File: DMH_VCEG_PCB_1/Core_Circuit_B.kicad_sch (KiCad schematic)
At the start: 83 parts, among them Q5 BC548, Q6 BC558, Q7 BC548, SW2 SW_DPDT_x2, U10 TL074, U11 4001, U12 40106, U13 CD4066BE, U14 TL074, U15 TL074, U16 TL074

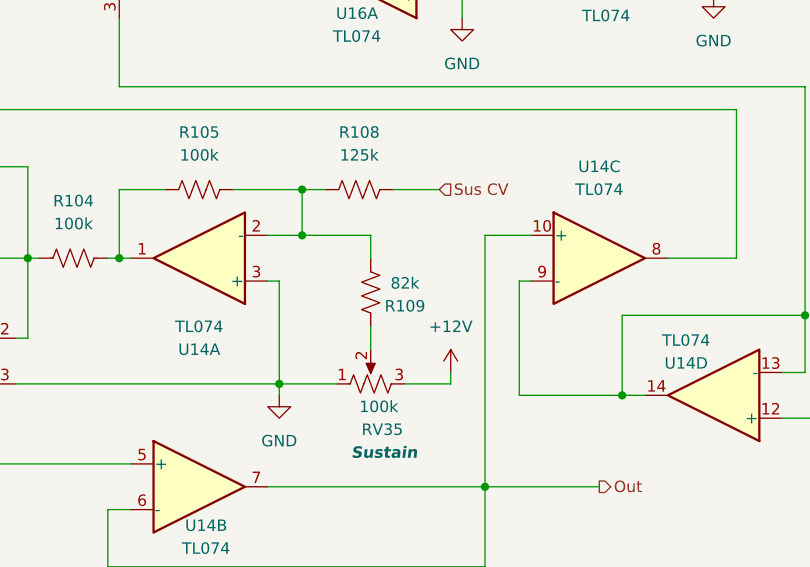
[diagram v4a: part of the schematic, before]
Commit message: Updated SG Out circuit
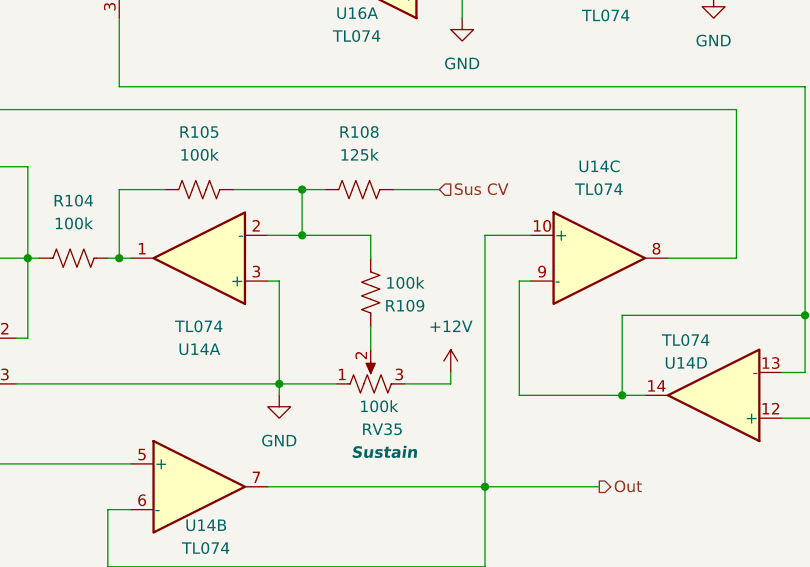
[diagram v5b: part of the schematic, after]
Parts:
- R109: value 82k -> 100k
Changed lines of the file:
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@@
 			)
 		)
-		(property "Value" "82k"
+		(property "Value" "100k"
 			(at 194.31 133.604 0)
 			(effects

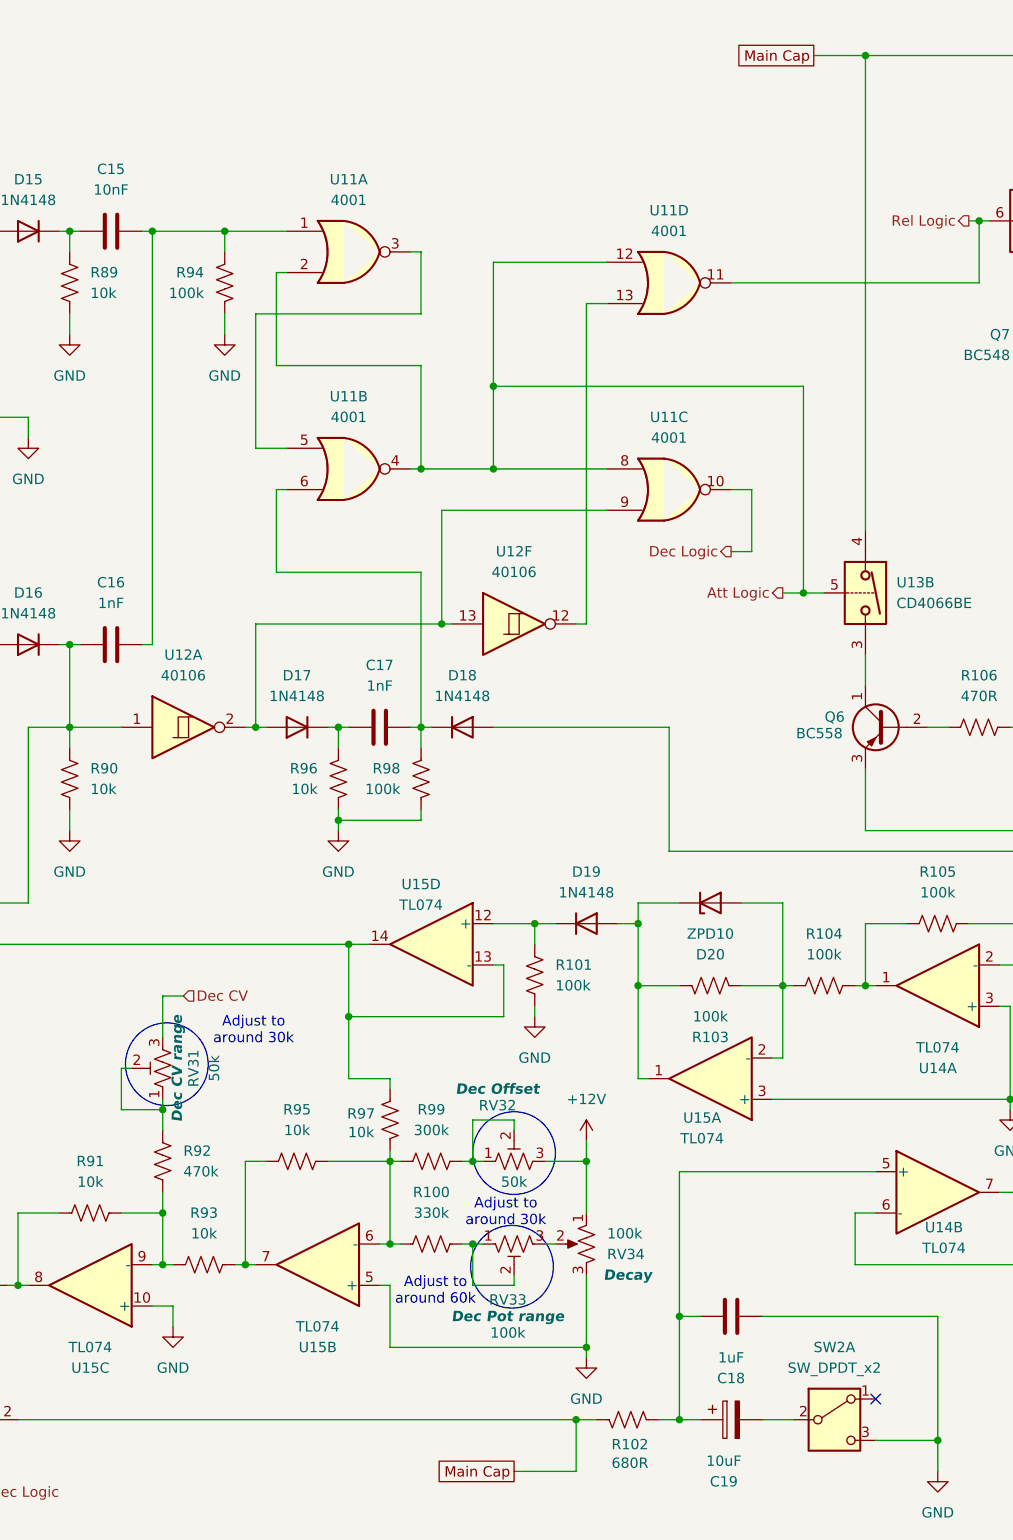
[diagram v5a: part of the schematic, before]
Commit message: Added Loop circuit
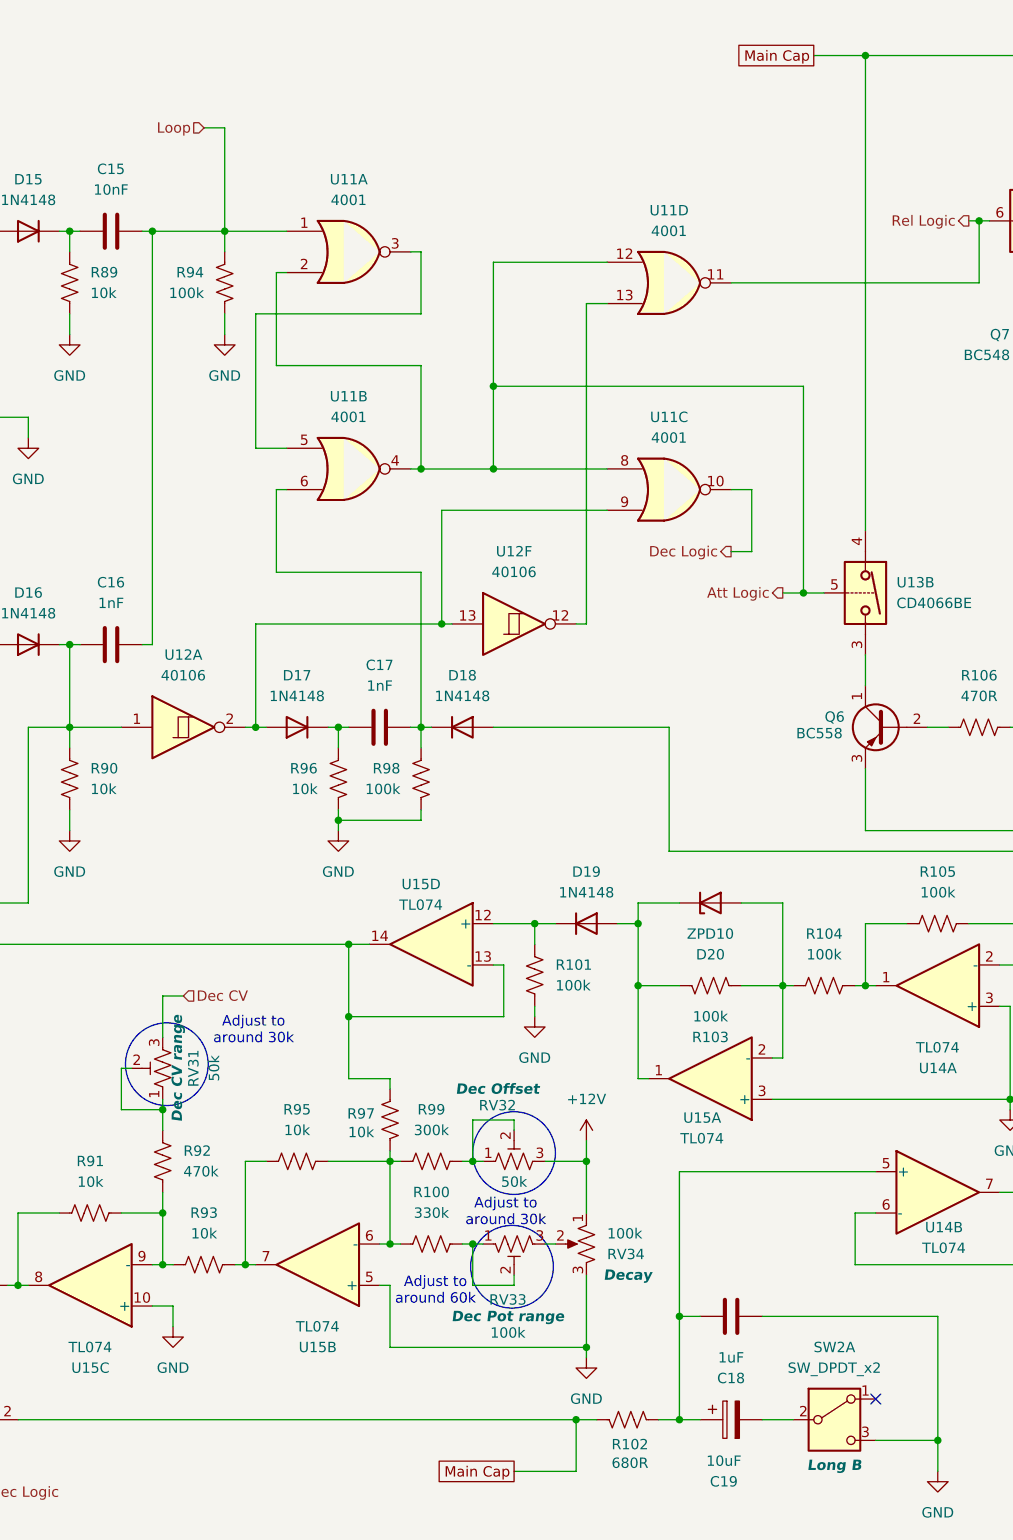
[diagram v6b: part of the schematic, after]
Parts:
- SW2: Function (none) -> Long B
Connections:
- net Loop: now reaches C15.2, C16.2, R94.2, U11.1
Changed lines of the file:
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@@
 	(wire
 		(pts
+			(xy 81.28 25.4) (xy 83.82 25.4)
+		)
+		(stroke
+			(width 0)
+			(type default)
+		)
+	)
+	(wire
+		(pts
 			(xy 54.61 88.9) (xy 55.88 88.9)
 		)
@@
 	(wire
 		(pts
+			(xy 83.82 25.4) (xy 83.82 38.1)
+		)
+		(stroke
+			(width 0)
+			(type default)
+		)
+	)
+	(wire
+		(pts
 			(xy 128.27 149.86) (xy 128.27 152.4)
 		)
@@
 		)
 	)
+	(hierarchical_label "Loop"
+		(shape input)
+		(at 81.28 25.4 180)
+		(effects
+			(font
+				(size 1.27 1.27)
+			)
+			(justify right)
+		)
+	)
 	(hierarchical_label "Trig"
 		(shape input)
@@
 		(on_board yes)
 		(dnp no)
-		(fields_autoplaced yes)
 		(property "Reference" "SW2"
 			(at 158.75 175.26 0)
@@
 			)
 		)
-		(property "Function" ""
-			(at 158.75 184.15 0)
+		(property "Function" "Long B"
+			(at 158.75 189.738 0)
 			(effects
 				(font
 					(size 1.27 1.27)
+					(thickness 0.254)
+					(bold yes)
+					(italic yes)
 				)
 			)

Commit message: PCB 1 ready for placement
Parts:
- added J25: Conn_01x10_PinHeader, symbol SynthStuff:Conn_01x10_PinHeader
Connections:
- net GND: now also J25.5 (Pin_5)
- net at RV43.3, RV44.2: now also J25.6 (Pin_6)
- net at C19.2, SW2.2 (B): now also J25.7 (Pin_7)
- net at RV33.3, RV34.2: now also J25.4 (Pin_4)
- net at RV39.3, RV40.2: now also J25.3 (Pin_3)
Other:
- moved on the sheet: RV34, RV40, RV44
